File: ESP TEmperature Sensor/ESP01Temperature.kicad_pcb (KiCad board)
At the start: 2 copper layers, 10 parts, among them K1 CONN_3, P1 CONN_4X2, P2 CONN_2, SW1 PROG, SW2 RESET, U1 DS18B20

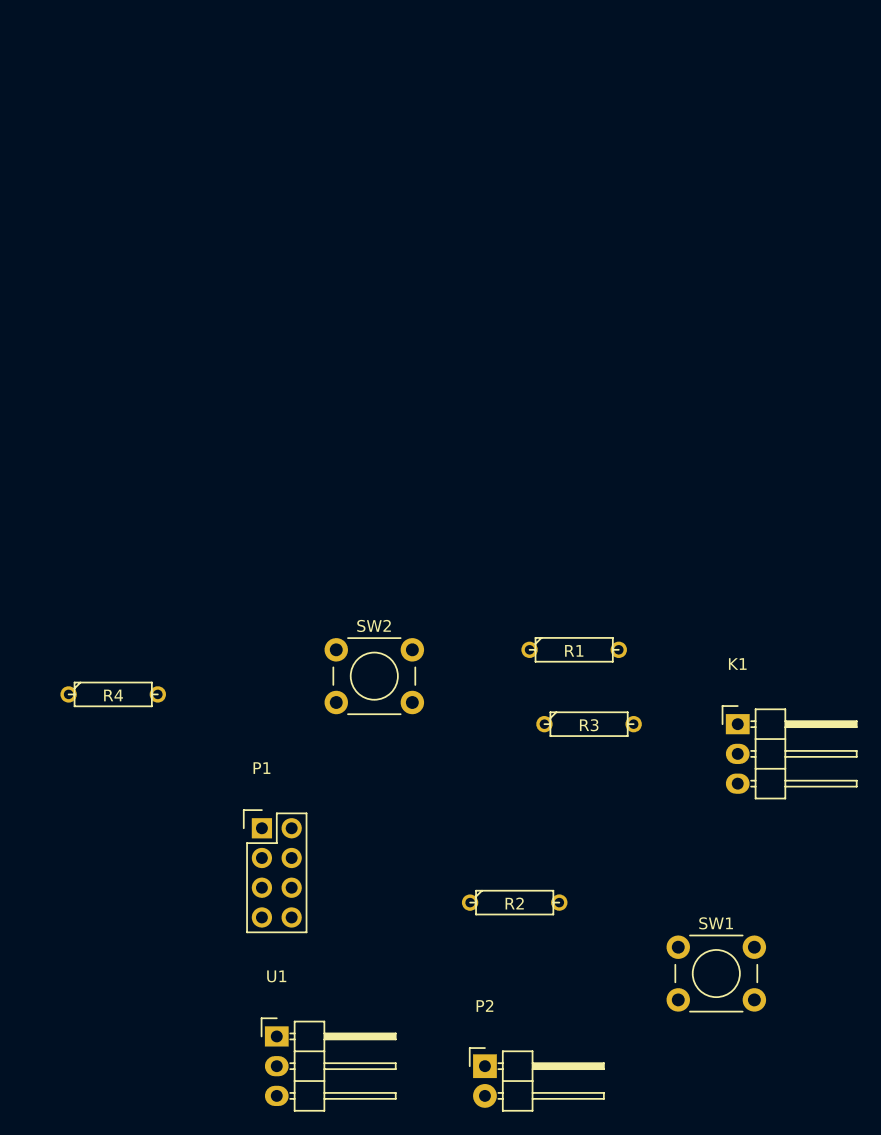
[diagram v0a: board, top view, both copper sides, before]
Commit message: PCB Design
Kicad design files for build PCB
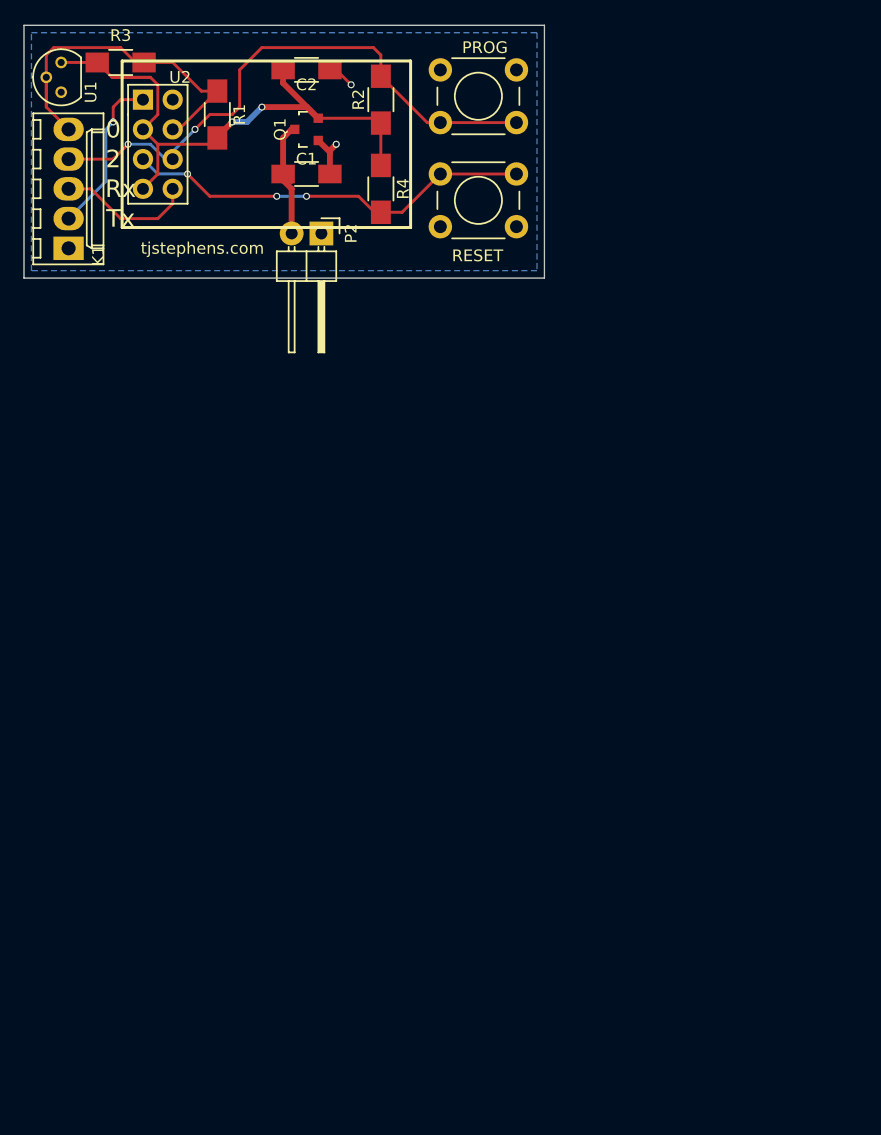
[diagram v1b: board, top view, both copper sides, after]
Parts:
- removed P1: CONN_4X2, Pin_Headers:Pin_Header_Straight_2x04
- added C1: 33u, Capacitors_SMD:C_1206_HandSoldering, F.Cu at (133.3, 49.5)
- added C2: 33u, Capacitors_SMD:C_1206_HandSoldering, F.Cu at (133.3, 40.6)
- added Q1: MCP1700T-3302E/TT, TO_SOT_Packages_SMD:SOT-23, F.Cu at (133.3, 45.7)
- added U2: ESP-01v090, ESP8266:ESP-01, F.Cu at (119.4, 43.2)
- K1: value CONN_3 -> CONN_5; footprint Pin_Headers:Pin_Header_Angled_1x03 -> Connectors_Molex:Molex_KK-6410-05_05x2.54mm_Straight
- R1, R2, R3, R4: footprint Discret:R3 -> Resistors_SMD:R_1206_HandSoldering
- U1: footprint Pin_Headers:Pin_Header_Angled_1x03 -> TO_SOT_Packages_THT:TO-92_Molded_Narrow
- moved U1 82.7 mm to (112.4, 42.5), turned to 90 degrees
- moved SW1 77.6 mm to (144.8, 40.6)
- moved P2 72.5 mm to (134.6, 54.6), turned to 270 degrees
- moved K1 70.1 mm to (113.0, 55.9), turned to 90 degrees
- moved R2 69.5 mm to (139.7, 43.2), turned to 90 degrees
- moved R3 69.2 mm to (117.5, 40.0)
- moved R1 54.9 mm to (125.7, 44.5), turned to 90 degrees
- moved R4 48.9 mm to (139.7, 50.8), turned to 270 degrees
- moved SW2 41.6 mm to (144.8, 49.5)
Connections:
- net /RESET renamed Net-(R4-Pad2)
- P2 pad 2: VDD -> Net-(C1-Pad1)
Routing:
- net VDD: track 0.00 -> 54.8 mm, vias 0 -> 2
- net /GPIO0: track 0.00 -> 49.2 mm, vias 0 -> 2
- net Net-(R4-Pad2): track 0.00 -> 35.7 mm, vias 0 -> 3
- net /GPIO2: track 0.00 -> 32.3 mm, vias 0 -> 1
- net /TX: track 0.00 -> 13.9 mm, vias 0 -> 1
- net /RX: track 0.00 -> 11.7 mm
- net Net-(C1-Pad1): track 0.00 -> 11.2 mm
- net GND: track 0.00 -> 6.51 mm, vias 0 -> 2
- added copper zone on B.Cu, net GND
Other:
- board outline added: 44.4 x 21.6 mm
- net class Power added: clearance 0.2, trace_width 0.5, via_dia 0.6, via_drill 0.4
- rule pad_to_mask_clearance: 0.2 -> 0
- board text added: "0"
- board text added: "2"
- board text added: "Rx"
- board text added: "Tx"
- board text added: "tjstephens.com"
